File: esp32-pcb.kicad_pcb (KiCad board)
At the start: 2 copper layers, 25.2 x 59.4 mm, 51 parts, among them J1 Conn_01x15_Male, J2 Conn_01x15_Male, Q1 SI2333DDS-T1-GE3, Q2 BSS138Q-7-F, Q3 MMBT3904, Q4 MMBT3904, Q5 BSS138Q-7-F, SW1 RESET, SW2 USER, SW3 SW_DIP_x04, U1 TLV75533, U2 ESP32-WROOM-32, U3 CP2102N-A01-GQFN24

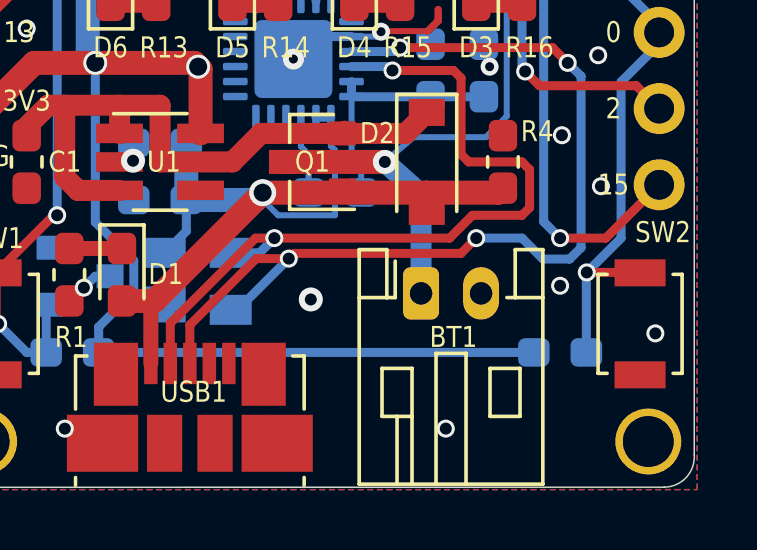
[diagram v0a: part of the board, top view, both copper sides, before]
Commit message: Add clear battery polarization indicators to the silkscreen. Bump revision to v2.0
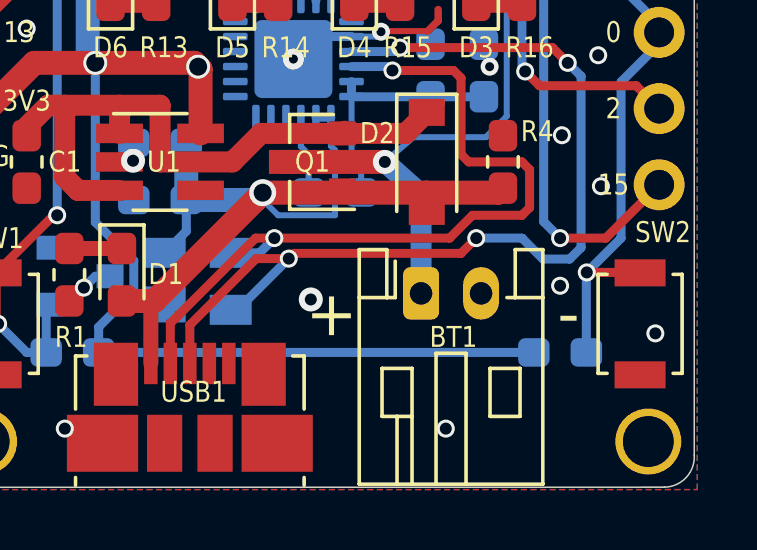
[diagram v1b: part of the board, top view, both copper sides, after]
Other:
- board text added: "+"
- board text added: "-"
- board text added: "DOGE32 v2.0"
- board text removed: "DOGE32 v1.0"
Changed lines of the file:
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@@
   (general
     (thickness 1.6)
-    (drawings 3060)
+    (drawings 3062)
     (tracks 624)
     (zones 0)
@@
     )
   )
+  (gr_text - (at 150.14 121.92) (layer F.SilkS)
+    (effects (font (size 1.5 1.5) (thickness 0.16)))
+  )
+  (gr_text + (at 142.24 121.92) (layer F.SilkS)
+    (effects (font (size 1.5 1.5) (thickness 0.16)))
+  )
   (gr_text 33 (at 147.828 108.712) (layer F.SilkS)
     (effects (font (size 0.7 0.6) (thickness 0.15)))
@@
     (effects (font (size 0.75 0.75) (thickness 0.15)) (justify mirror))
   )
-  (gr_text "DOGE32 v1.0" (at 137.414 93.853) (layer B.SilkS)
+  (gr_text "DOGE32 v2.0" (at 137.414 93.853) (layer B.SilkS)
     (effects (font (size 1 1) (thickness 0.15)) (justify mirror))
   )

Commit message: Use 1k resistor instead of 2k for green PWR led
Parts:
- removed ?: , 
- R1: value 2k -> 1k
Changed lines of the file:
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@@
     (tracks 624)
     (zones 0)
-    (modules 51)
+    (modules 50)
     (nets 75)
   )
@@
     (add_net V_BAT_MEASURE)
   )
-  (module "" (layer F.Cu)
-    (at 134.62 108.458)
-    (fp_text reference "" (at 133.858 120.65) (layer F.SilkS)
-      (effects (font (size 1.27 1.27) (thickness 0.15)))
-    )
-    (fp_text value "" (at 133.858 120.65) (layer F.SilkS)
-      (effects (font (size 1.27 1.27) (thickness 0.15)))
-    )
-  )
   (module Package_TO_SOT_SMD:SOT-23 (layer B.Cu)
     (at 133.858 120.65)
@@
       (effects (font (size 0.7 0.6) (thickness 0.16)))
     )
-    (fp_text value 2k (at 0 1.43 270) (layer F.Fab)
-      (effects (font (size 1 1) (thickness 0.15)))
-    )
+    (fp_text value 1k (at 0 1.43 270) (layer F.Fab)
+      (effects (font (size 1 1) (thickness 0.15)))
+    )

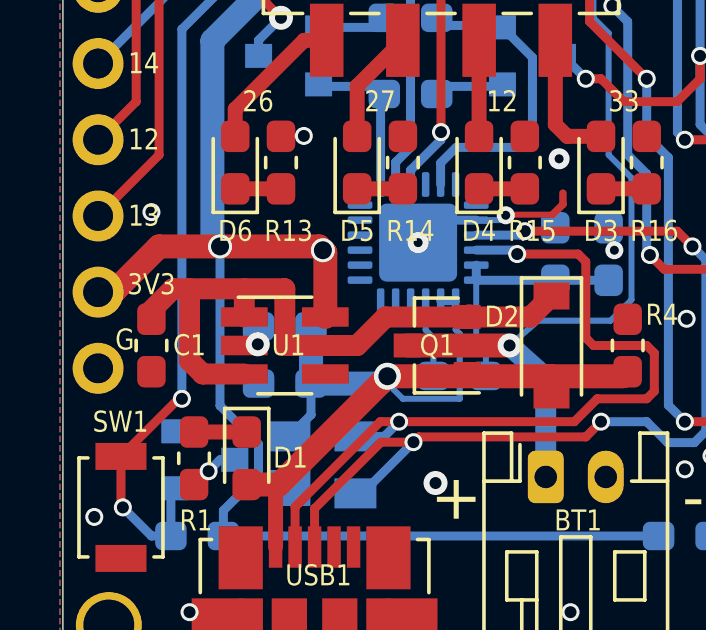
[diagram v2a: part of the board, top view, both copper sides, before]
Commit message: Use XC6220B331MR
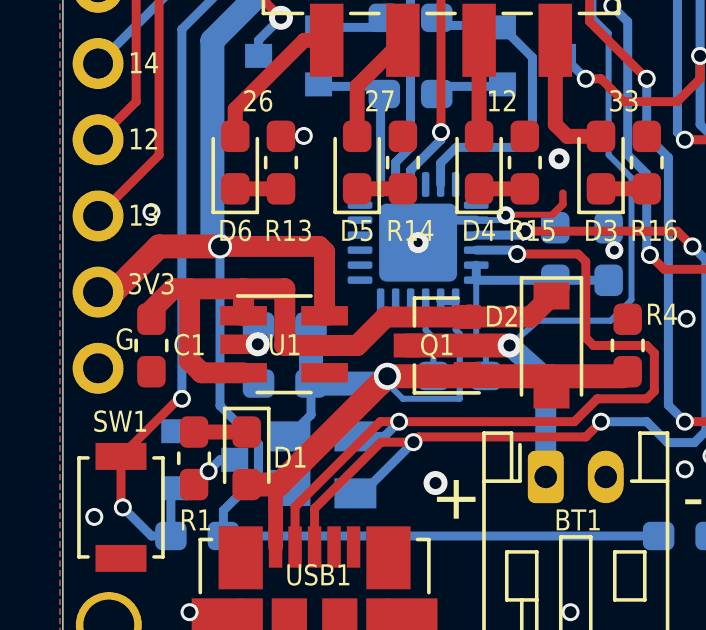
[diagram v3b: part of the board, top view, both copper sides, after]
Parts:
- U1: value TLV75533 -> XC6220B331MR
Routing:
- net 3V3: vias 3 -> 2
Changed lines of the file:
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@@
     (thickness 1.6)
     (drawings 3062)
-    (tracks 624)
+    (tracks 623)
     (zones 0)
     (modules 50)
@@
   )
   (setup
-    (last_trace_width 0.25)
+    (last_trace_width 0.7)
     (user_trace_width 0.2)
     (user_trace_width 0.25)
@@
     (add_net V_BAT_MEASURE)
   )
+  (module Package_TO_SOT_SMD:SOT-23-5_HandSoldering (layer F.Cu)
+    (at 136.5 116.8)
+    (descr "5-pin SOT23 package")
+    (tags "SOT-23-5 hand-soldering")
+    (attr smd)
+    (fp_text reference U1 (at 0.025 0.04) (layer F.SilkS)
+      (effects (font (size 0.7 0.6) (thickness 0.15)))
+    )
+    (fp_text value XC6220B331MR (at 0 2.9) (layer F.Fab)
+      (effects (font (size 1 1) (thickness 0.15)))
+    )
+    (fp_line (start 2.38 1.8) (end -2.38 1.8) (layer F.CrtYd) (width 0.05))
+    (fp_line (start 2.38 1.8) (end 2.38 -1.8) (layer F.CrtYd) (width 0.05))
+    (fp_line (start -2.38 -1.8) (end -2.38 1.8) (layer F.CrtYd) (width 0.05))
+    (fp_line (start -2.38 -1.8) (end 2.38 -1.8) (layer F.CrtYd) (width 0.05))
+    (fp_line (start 0.9 -1.55) (end 0.9 1.55) (layer F.Fab) (width 0.1))
+    (fp_line (start 0.9 1.55) (end -0.9 1.55) (layer F.Fab) (width 0.1))
+    (fp_line (start -0.9 -0.9) (end -0.9 1.55) (layer F.Fab) (width 0.1))
+    (fp_line (start 0.9 -1.55) (end -0.25 -1.55) (layer F.Fab) (width 0.1))
+    (fp_line (start -0.9 -0.9) (end -0.25 -1.55) (layer F.Fab) (width 0.1))
+    (fp_line (start 0.9 -1.61) (end -1.55 -1.61) (layer F.SilkS) (width 0.12))
+    (fp_line (start -0.9 1.61) (end 0.9 1.61) (layer F.SilkS) (width 0.12))
+    (fp_text user %R (at 0 0 90) (layer F.Fab)
+      (effects (font (size 0.5 0.5) (thickness 0.075)))
+    )
+    (pad 5 smd rect (at 1.35 -0.95) (size 1.56 0.65) (layers F.Cu F.Paste F.Mask)
+      (net 3 3V3))
+    (pad 4 smd rect (at 1.35 0.95) (size 1.56 0.65) (layers F.Cu F.Paste F.Mask)
+      (net 49 "Net-(U1-Pad4)"))
+    (pad 3 smd rect (at -1.35 0.95) (size 1.56 0.65) (layers F.Cu F.Paste F.Mask)
+      (net 72 "Net-(C1-Pad1)"))
+    (pad 2 smd rect (at -1.35 0) (size 1.56 0.65) (layers F.Cu F.Paste F.Mask)
+      (net 1 GND))
+    (pad 1 smd rect (at -1.35 -0.95) (size 1.56 0.65) (layers F.Cu F.Paste F.Mask)
+      (net 72 "Net-(C1-Pad1)"))
+    (model ${KISYS3DMOD}/Package_TO_SOT_SMD.3dshapes/SOT-23-5.wrl
+      (at (xyz 0 0 0))
+      (scale (xyz 1 1 1))
+      (rotate (xyz 0 0 0))
+    )
+  )
   (module Package_TO_SOT_SMD:SOT-23 (layer B.Cu)
     (at 133.858 120.65)
@@
     )
   )
-  (module Package_TO_SOT_SMD:SOT-23-5_HandSoldering (layer F.Cu)
-    (at 136.525 116.84)
-    (descr "5-pin SOT23 package")
-    (tags "SOT-23-5 hand-soldering")
-    (attr smd)
-    (fp_text reference U1 (at 0.127 0) (layer F.SilkS)
-      (effects (font (size 0.7 0.6) (thickness 0.16)))
-    )
-    (fp_text value TLV75533 (at 0 2.9) (layer F.Fab)
-      (effects (font (size 1 1) (thickness 0.15)))
-    )
-    (fp_line (start 2.38 1.8) (end -2.38 1.8) (layer F.CrtYd) (width 0.05))
-    (fp_line (start 2.38 1.8) (end 2.38 -1.8) (layer F.CrtYd) (width 0.05))
-    (fp_line (start -2.38 -1.8) (end -2.38 1.8) (layer F.CrtYd) (width 0.05))
-    (fp_line (start -2.38 -1.8) (end 2.38 -1.8) (layer F.CrtYd) (width 0.05))
-    (fp_line (start 0.9 -1.55) (end 0.9 1.55) (layer F.Fab) (width 0.1))
-    (fp_line (start 0.9 1.55) (end -0.9 1.55) (layer F.Fab) (width 0.1))
-    (fp_line (start -0.9 -0.9) (end -0.9 1.55) (layer F.Fab) (width 0.1))
-    (fp_line (start 0.9 -1.55) (end -0.25 -1.55) (layer F.Fab) (width 0.1))
-    (fp_line (start -0.9 -0.9) (end -0.25 -1.55) (layer F.Fab) (width 0.1))
-    (fp_line (start 0.9 -1.61) (end -1.55 -1.61) (layer F.SilkS) (width 0.12))
-    (fp_line (start -0.9 1.61) (end 0.9 1.61) (layer F.SilkS) (width 0.12))
-    (fp_text user %R (at 0 0 90) (layer F.Fab)
-      (effects (font (size 0.7 0.6) (thickness 0.16)))
-    )
-    (pad 5 smd rect (at 1.35 -0.95) (size 1.56 0.65) (layers F.Cu F.Paste F.Mask)
-      (net 3 3V3))
-    (pad 4 smd rect (at 1.35 0.95) (size 1.56 0.65) (layers F.Cu F.Paste F.Mask)
-      (net 49 "Net-(U1-Pad4)"))
-    (pad 3 smd rect (at -1.35 0.95) (size 1.56 0.65) (layers F.Cu F.Paste F.Mask)
-      (net 72 "Net-(C1-Pad1)"))
-    (pad 2 smd rect (at -1.35 0) (size 1.56 0.65) (layers F.Cu F.Paste F.Mask)
-      (net 1 GND))
-    (pad 1 smd rect (at -1.35 -0.95) (size 1.56 0.65) (layers F.Cu F.Paste F.Mask)
-      (net 72 "Net-(C1-Pad1)"))
-    (model ${KISYS3DMOD}/Package_TO_SOT_SMD.3dshapes/SOT-23-5.wrl
-      (at (xyz 0 0 0))
-      (scale (xyz 1 1 1))
-      (rotate (xyz 0 0 0))
-    )
-  )
   (module Connector_JST:JST_PH_S2B-PH-K_1x02_P2.00mm_Horizontal (layer F.Cu)
     (at 145.2245 121.2215)
@@
   (via (at 141.605 102.235) (size 0.6) (drill 0.4) (layers F.Cu B.Cu) (net 1))
   (via (at 131.445 100.965) (size 0.6) (drill 0.4) (layers F.Cu B.Cu) (net 1))
-  (via (at 132.08 112.395) (size 0.6) (drill 0.4) (layers F.Cu B.Cu) (net 1))
   (via (at 137.16 109.855) (size 0.6) (drill 0.4) (layers F.Cu B.Cu) (net 1))
   (via (at 153.035 122.555) (size 0.6) (drill 0.4) (layers F.Cu B.Cu) (net 1))
@@
   (via (at 130.175 122.555) (size 0.6) (drill 0.4) (layers F.Cu B.Cu) (net 1))
   (via (at 137.795 78.105) (size 0.6) (drill 0.4) (layers F.Cu B.Cu) (net 1))
+  (via (at 132.08 112.395) (size 0.6) (drill 0.4) (layers F.Cu B.Cu) (net 1))
   (via (at 144.272 85.344) (size 0.6) (drill 0.4) (layers F.Cu B.Cu) (net 2))
   (via (at 143.764 90.424) (size 0.6) (drill 0.4) (layers F.Cu B.Cu) (net 2))
@@
   (segment (start 130.048 81.788) (end 130.302 82.042) (width 0.8) (layer F.Cu) (net 3) (status 30))
   (segment (start 130.048 78.345) (end 130.048 81.788) (width 0.8) (layer F.Cu) (net 3) (status 30))
-  (segment (start 137.795 113.665) (end 137.875 113.745) (width 0.8) (layer F.Cu) (net 3))
-  (via (at 137.795 113.665) (size 0.8) (drill 0.6) (layers F.Cu B.Cu) (net 3))
-  (segment (start 137.875 113.745) (end 137.875 115.89) (width 0.8) (layer F.Cu) (net 3) (status 20))
   (segment (start 148.985 123.19) (end 134.479 123.19) (width 0.3) (layer B.Cu) (net 3) (status 30))
   (via (at 138.246171 81.473062) (size 0.9) (drill 0.6) (layers F.Cu B.Cu) (net 3))
@@
   (segment (start 138.246171 81.473062) (end 138.230611 81.473062) (width 0.8) (layer F.Cu) (net 3))
   (segment (start 135.116549 78.359) (end 133.232 78.359) (width 0.8) (layer F.Cu) (net 3) (status 20))
-  (segment (start 137.668 113.538) (end 137.795 113.665) (width 0.8) (layer F.Cu) (net 3))
   (segment (start 130.302 115.062) (end 130.81 115.062) (width 0.8) (layer F.Cu) (net 3) (status 30))
   (segment (start 130.81 115.062) (end 132.334 113.538) (width 0.8) (layer F.Cu) (net 3) (status 10))
-  (via (at 134.366 113.538) (size 0.8) (drill 0.6) (layers F.Cu B.Cu) (net 3))
   (segment (start 132.334 113.538) (end 134.366 113.538) (width 0.8) (layer F.Cu) (net 3))
-  (segment (start 134.366 113.538) (end 137.668 113.538) (width 0.8) (layer F.Cu) (net 3))
   (segment (start 134.479 113.651) (end 134.366 113.538) (width 0.3) (layer B.Cu) (net 3))
   (segment (start 139.95797 83.184861) (end 139.95797 96.26203) (width 0.8) (layer B.Cu) (net 3))
@@
   (segment (start 134.479 123.19) (end 134.479 122.3404) (width 0.3) (layer B.Cu) (net 3) (status 10))
   (segment (start 135.6487 121.1707) (end 135.6487 120.1293) (width 0.3) (layer B.Cu) (net 3))
+  (segment (start 137.85 115.85) (end 137.85 113.72) (width 0.7) (layer F.Cu) (net 3))
+  (segment (start 137.668 113.538) (end 137.85 113.72) (width 0.7) (layer F.Cu) (net 3))
+  (segment (start 134.366 113.538) (end 137.668 113.538) (width 0.7) (layer F.Cu) (net 3))
+  (via (at 134.366 113.538) (size 0.8) (drill 0.6) (layers F.Cu B.Cu) (net 3))
   (segment (start 142.9135 114.667) (end 142.9075 114.661) (width 0.3) (layer B.Cu) (net 4) (status 30))
   (segment (start 145.542 114.667) (end 142.9135 114.667) (width 0.3) (layer B.Cu) (net 4) (status 30))
@@
   (segment (start 140.989883 119.888) (end 140.814952 120.062931) (width 0.3) (layer F.Cu) (net 69))
   (segment (start 146.558 119.888) (end 140.989883 119.888) (width 0.3) (layer F.Cu) (net 69))
-  (segment (start 132.08 115.965) (end 132.08 115.67) (width 0.5) (layer F.Cu) (net 72) (status 30))
   (segment (start 132.08 115.67) (end 132.8 114.95) (width 0.7) (layer F.Cu) (net 72) (status 10))
   (segment (start 136.525 114.95) (end 136.525 116.84) (width 0.7) (layer F.Cu) (net 72))
-  (segment (start 135.175 115.89) (end 135.175 114.95) (width 0.7) (layer F.Cu) (net 72) (status 10))
   (segment (start 133.35 117.348) (end 133.35 114.95) (width 0.7) (layer F.Cu) (net 72))
-  (segment (start 135.175 117.79) (end 133.792 117.79) (width 0.7) (layer F.Cu) (net 72) (status 10))
-  (segment (start 133.792 117.79) (end 133.35 117.348) (width 0.7) (layer F.Cu) (net 72))
-  (segment (start 132.8 114.95) (end 136.525 114.95) (width 0.7) (layer F.Cu) (net 72))
   (segment (start 142.68 115.815) (end 142.605 115.89) (width 0.7) (layer F.Cu) (net 72) (status 30))
   (segment (start 142.605 115.89) (end 139.888 115.89) (width 0.7) (layer F.Cu) (net 72) (status 10))
@@
   (segment (start 144.715 115.89) (end 145.415 115.19) (width 0.7) (layer F.Cu) (net 72) (status 20))
   (segment (start 142.605 115.89) (end 144.715 115.89) (width 0.7) (layer F.Cu) (net 72) (status 10))
+  (segment (start 135.15 115.85) (end 135.15 114.95) (width 0.7) (layer F.Cu) (net 72))
+  (segment (start 132.8 114.95) (end 135.15 114.95) (width 0.7) (layer F.Cu) (net 72))
+  (segment (start 135.15 114.95) (end 136.525 114.95) (width 0.7) (layer F.Cu) (net 72))
+  (segment (start 133.752 117.75) (end 133.35 117.348) (width 0.7) (layer F.Cu) (net 72))
+  (segment (start 135.15 117.75) (end 133.752 117.75) (width 0.7) (layer F.Cu) (net 72))
+  (segment (start 132.08 115.965) (end 132.08 115.67) (width 0.5) (layer F.Cu) (net 72) (status 30))
   (segment (start 133.232 79.629) (end 134.747 79.629) (width 0.3) (layer F.Cu) (net 73) (status 10))
   (segment (start 137.668 82.122773) (end 135.174227 79.629) (width 0.3) (layer F.Cu) (net 73))

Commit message: Use 30k resistor for R7 so that 0.75 * VBAT is dropped at it instead of 0.5*VBAT. This should improve battery reading precision
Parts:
- R7: value 10k -> 30k
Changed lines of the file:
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@@
   )
   (setup
-    (last_trace_width 0.7)
+    (last_trace_width 0.25)
     (user_trace_width 0.2)
     (user_trace_width 0.25)
@@
       (effects (font (size 0.7 0.6) (thickness 0.16)) (justify mirror))
     )
-    (fp_text value 10k (at 0 -1.43 180) (layer B.Fab)
+    (fp_text value 30k (at 0 -1.43 180) (layer B.Fab)
       (effects (font (size 1 1) (thickness 0.15)) (justify mirror))
     )
